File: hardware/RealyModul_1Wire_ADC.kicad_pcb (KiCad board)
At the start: 2 copper layers, 90.2 x 80 mm, 69 parts, among them J1 Conn_01x03, J10 1Wire, J11 1Wire, J2 1Wire, J3 Conn_01x03, J4 Conn_01x03, J5 1Wire, J6 1Wire, J7 1Wire, J8 1Wire, J9 1Wire, K1 RT314A12, K2 RT314A12, K3 RT314A12, Q1 BSS123, Q2 BSS123, Q3 BSS123, U1 LT1129-3.3_SOT223, U2 R-78B5.0-2.0, U3 ESP32-WROOM-32D, U4 ADS1115IDGS

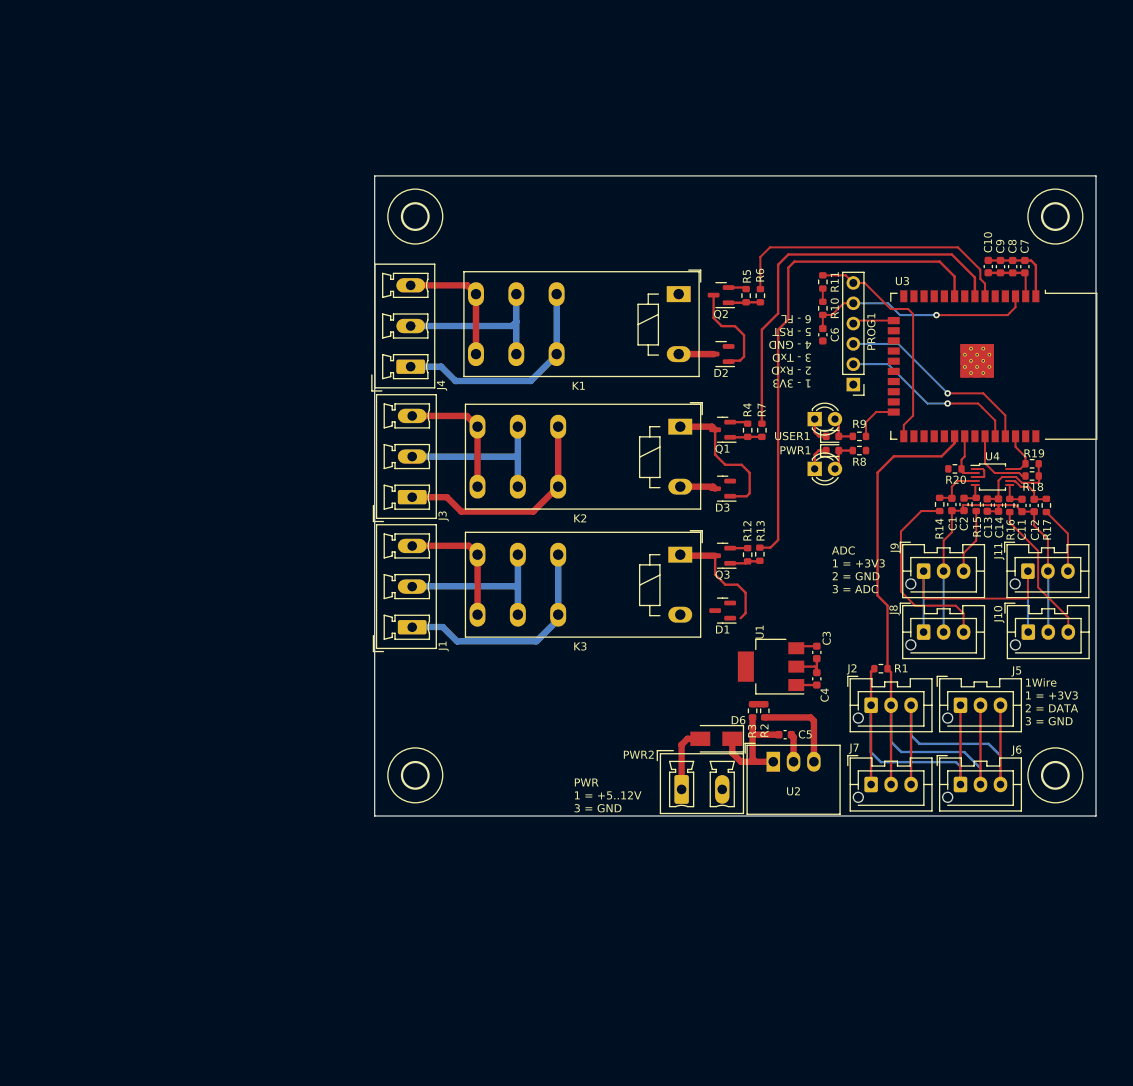
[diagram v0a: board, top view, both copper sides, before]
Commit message: Schaltplan angepasst
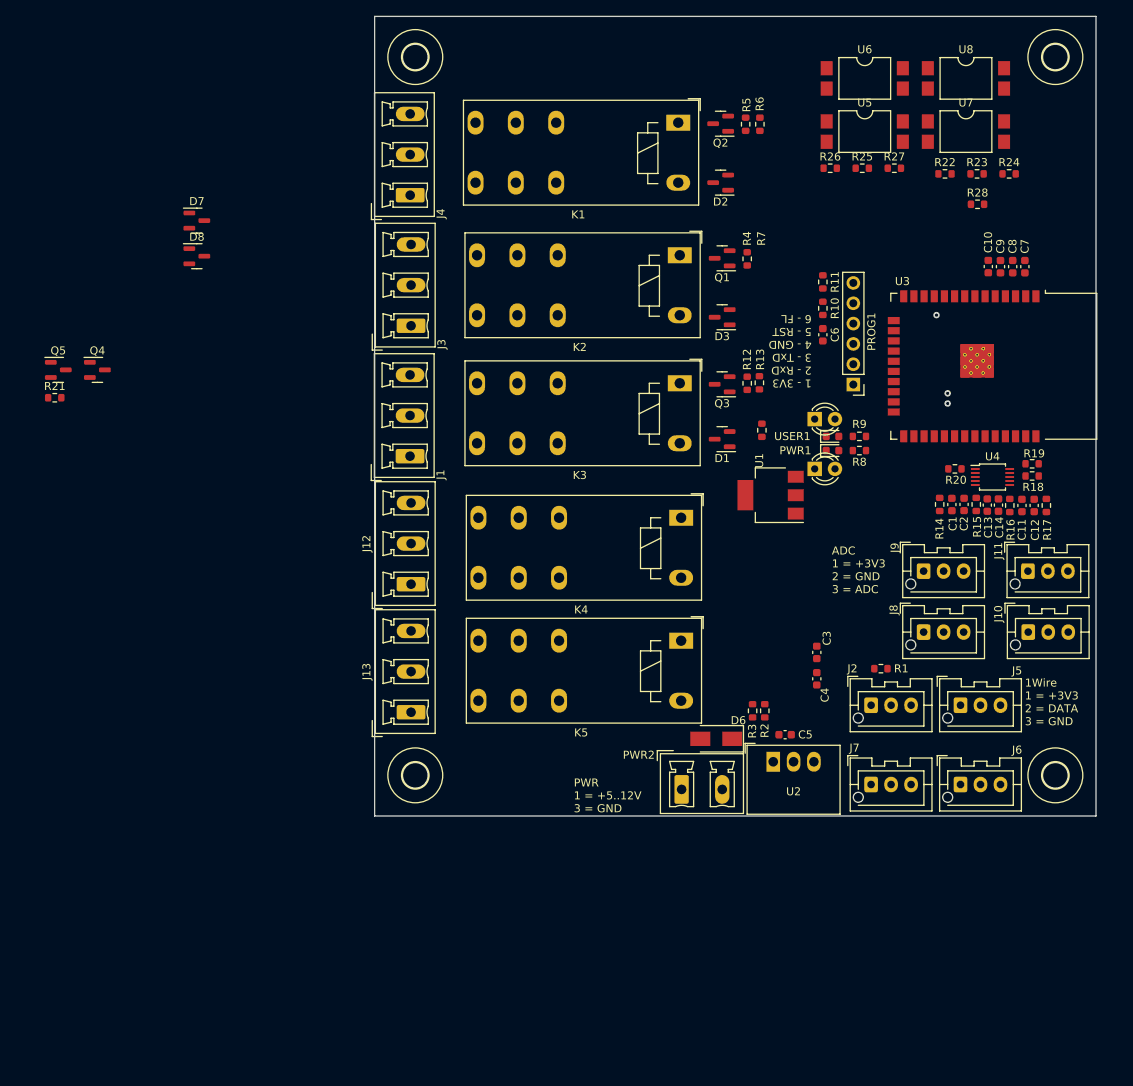
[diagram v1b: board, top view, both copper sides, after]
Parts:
- added D7: BAS21, Package_TO_SOT_SMD:SOT-23, F.Cu at (92.1, 65.3)
- added D8: BAS21, Package_TO_SOT_SMD:SOT-23, F.Cu at (92.1, 69.7)
- added J12: Conn_01x03, Connector_Phoenix_MC_HighVoltage:PhoenixContact_MCV_1,5_3-G-5.08_1x03_P5.08mm_Vertical, F.Cu at (118.9, 110.7)
- added J13: Conn_01x03, Connector_Phoenix_MC_HighVoltage:PhoenixContact_MCV_1,5_3-G-5.08_1x03_P5.08mm_Vertical, F.Cu at (118.9, 126.7)
- added K4: RT314A12, Relay_THT:Relay_SPDT_Schrack-RT1-16A-FormC_RM5mm, F.Cu at (152.6, 102.4)
- added K5: RT314A12, Relay_THT:Relay_SPDT_Schrack-RT1-16A-FormC_RM5mm, F.Cu at (152.6, 117.8)
- added Q4: BSS123, Package_TO_SOT_SMD:SOT-23, F.Cu at (79.6, 83.9)
- added Q5: BSS123, Package_TO_SOT_SMD:SOT-23, F.Cu at (74.8, 83.9)
- added R21: 100k, Resistor_SMD:R_0603_1608Metric, F.Cu at (74.3, 87.4)
- added R22: 100k, Resistor_SMD:R_0603_1608Metric, F.Cu at (185.6, 59.4)
- added R23: 100, Resistor_SMD:R_0603_1608Metric, F.Cu at (189.6, 59.4)
- added R24: 100, Resistor_SMD:R_0603_1608Metric, F.Cu at (193.6, 59.4)
- added R25: 10k, Resistor_SMD:R_0603_1608Metric, F.Cu at (175.3, 58.7)
- added R26: 10k, Resistor_SMD:R_0603_1608Metric, F.Cu at (171.2, 58.7)
- added R27: 10k, Resistor_SMD:R_0603_1608Metric, F.Cu at (179.3, 58.7)
- added R28: 10k, Resistor_SMD:R_0603_1608Metric, F.Cu at (189.7, 63.2)
- added U5: SFH6206-1T, Package_DIP:SMDIP-4_W9.53mm_Clearance8mm, F.Cu at (175.6, 54.1)
- added U6: SFH6206-1T, Package_DIP:SMDIP-4_W9.53mm_Clearance8mm, F.Cu at (175.6, 47.5)
- added U7: SFH6206-1T, Package_DIP:SMDIP-4_W9.53mm_Clearance8mm, F.Cu at (188.2, 54.1)
- added U8: SFH6206-1T, Package_DIP:SMDIP-4_W9.53mm_Clearance8mm, F.Cu at (188.2, 47.5)
- R12: value 100k -> 0R0
- R13: value 100 -> N.P.
- R2: value 0R0 -> 100k
- R3: value N.P. -> 100k
- R5: value 100k -> 100
- moved J3 21.4 mm to (118.9, 78.4)
- moved K1 21.4 mm to (152.3, 53.0)
- moved Q2 21.4 mm to (157.5, 53.2)
- moved R5 21.4 mm to (160.7, 53.2)
- moved R6 21.4 mm to (162.5, 53.2)
- moved D1 21.4 mm to (157.7, 92.6)
- moved D2 21.4 mm to (157.5, 60.5)
- moved D3 21.4 mm to (157.7, 77.4)
- moved K2 21.4 mm to (152.4, 69.6)
- moved K3 21.4 mm to (152.4, 85.6)
- moved Q1 21.4 mm to (157.7, 70.0)
- moved Q3 21.4 mm to (157.7, 85.7)
- moved R12 21.4 mm to (160.9, 85.6)
- moved R13 21.4 mm to (162.4, 85.6)
- moved R4 21.4 mm to (160.9, 70.1)
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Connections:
- K1 pad 11: Net-(J4-Pad2) -> Net-(J1-Pad2)
- K1 pad 12: Net-(J4-Pad1) -> Net-(J1-Pad1)
- K1 pad 14: Net-(J4-Pad3) -> Net-(J1-Pad3)
- K1 pad A1: Net-(D2-Pad1) -> Net-(D1-Pad1)
- K2 pad 11: Net-(J3-Pad2) -> Net-(J4-Pad2)
- K2 pad 12: Net-(J3-Pad1) -> Net-(J4-Pad1)
- K2 pad 14: Net-(J3-Pad3) -> Net-(J4-Pad3)
- K2 pad A1: Net-(D3-Pad1) -> Net-(D2-Pad1)
- K3 pad 11: Net-(J1-Pad2) -> Net-(J3-Pad2)
- K3 pad 12: Net-(J1-Pad1) -> Net-(J3-Pad1)
- K3 pad 14: Net-(J1-Pad3) -> Net-(J3-Pad3)
- K3 pad A1: Net-(D1-Pad1) -> Net-(D3-Pad1)
- Q1 pad 3: Net-(D3-Pad1) -> Net-(D1-Pad1)
- Q3 pad 3: Net-(D1-Pad1) -> Net-(D3-Pad1)
- R12 pad 1: Net-(Q3-Pad1) -> +5V
- R12 pad 2: GND -> Vdrive
- R13 pad 1: Net-(Q3-Pad1) -> +24V
- R13 pad 2: /IO33_K3 -> Vdrive
- R2 pad 1: +5V -> Net-(Q3-Pad1)
- R2 pad 2: Vdrive -> GND
- R3 pad 1: +24V -> Net-(Q2-Pad1)
- R3 pad 2: Vdrive -> GND
- R5 pad 1: Net-(Q2-Pad1) -> Net-(Q3-Pad1)
- R5 pad 2: GND -> /IO33_K3
- R6 pad 2: /IO34_K1 -> /IO35_K2
- R7 pad 2: /IO35_K2 -> /IO34_K1
- U3 pad 10: unconnected-(U3-Pad10) -> /IO25_K5
- U3 pad 11: unconnected-(U3-Pad11) -> /INPUT_01
- U3 pad 12: unconnected-(U3-Pad12) -> /INPUT_02
- U3 pad 13: unconnected-(U3-Pad13) -> /INPUT_03
- U3 pad 14: unconnected-(U3-Pad14) -> /INPUT_04
- U3 pad 8: unconnected-(U3-Pad8) -> /IO33_K3
- U3 pad 9: /IO33_K3 -> /IO32_K4
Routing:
- net GND: track 124.9 -> 0.00 mm
- net +3.3V: track 103.3 -> 0.00 mm
- net /1Wire: track 80.8 -> 0.00 mm
- net /IO33_K3: track 61.6 -> 0.00 mm
- net /IO35_K2: track 49.4 -> 0.00 mm
- net /IO34_K1: track 36.7 -> 0.00 mm
- net /IO0: track 29.0 -> 0.00 mm
- net /RST: track 28.8 -> 0.00 mm
- net Net-(J4-Pad1): track 28.0 -> 0.00 mm
- net Net-(J3-Pad1): track 27.8 -> 0.00 mm
- net Net-(J1-Pad1): track 27.6 -> 0.00 mm
- net /TXD: track 25.3 -> 0.00 mm
- net Net-(J8-Pad3): track 24.7 -> 0.00 mm
- net /RXD: track 22.6 -> 0.00 mm
- net Net-(J4-Pad2): track 20.9 -> 0.00 mm
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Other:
- board size 90.2 x 80 mm -> 90.2 x 99.9 mm

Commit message: änderung
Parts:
- removed D8: BAS21, Package_TO_SOT_SMD:SOT-23
- removed H1, H2, H3, H4: MOUNT-HOLE3.2, main:3,2
- removed J13: Conn_01x03, Connector_Phoenix_MC_HighVoltage:PhoenixContact_MCV_1,5_3-G-5.08_1x03_P5.08mm_Vertical
- removed J6, J7: 1Wire, Connector_JST:JST_XA_B03B-XASK-1-A_1x03_P2.50mm_Vertical
- removed K5: RT314A12, Relay_THT:Relay_SPDT_Schrack-RT1-16A-FormC_RM5mm
- removed Q5: BSS123, Package_TO_SOT_SMD:SOT-23
- removed R22: 100k, Resistor_SMD:R_0603_1608Metric
- removed R24: 100, Resistor_SMD:R_0603_1608Metric
- added PS3: IRM-05-5, Converter_ACDC:Converter_ACDC_MeanWell_IRM-05-xx_THT, F.Cu at (105.4, 93.5)
- D1, D2, D3, D7, Q1, Q2, Q3, Q4, R2, R21, R23, R3, R4, R5, R6, R7: moved to B.Cu
- moved U8 114.8 mm to (108.0, 129.5)
- moved U7 106.3 mm to (107.8, 123.7)
- moved U6 97.5 mm to (108.0, 117.7)
- moved D5 94.7 mm to (90.5, 142.6)
- moved PWR1 94.7 mm to (92.7, 146.6)
- moved USER1 94.7 mm to (92.7, 144.8)
- moved D4 94.7 mm to (90.5, 148.8)
- moved R9 94.7 mm to (96.1, 144.8)
- moved R8 94.7 mm to (96.1, 146.6)
- moved R25 91.5 mm to (115.8, 128.3), turned to 180 degrees
- moved U5 88.8 mm to (108.0, 111.8)
- moved R28 87.6 mm to (116.0, 110.5), turned to 180 degrees
- moved R27 85.7 mm to (116.0, 116.5), turned to 180 degrees
- moved R26 84.4 mm to (115.8, 122.4), turned to 180 degrees
- moved C7 80.2 mm to (156.0, 140.8), turned to 0 degrees
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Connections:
- R23 pad 2: /IO25_K5 -> /IO32_K4
- U3 pad 10: /IO25_K5 -> unconnected-(U3-IO25-Pad10)
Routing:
- net /TXD: vias 1 -> 0
- net /RXD: vias 1 -> 0
- net /RST: vias 1 -> 0
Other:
- board size 90.2 x 99.9 mm -> 86.4 x 103.6 mm

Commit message: fast fertig
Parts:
- removed C5: 100nF/50V, Capacitor_SMD:C_0603_1608Metric
- removed D6: ES1D, Diode_SMD:D_SMA
- removed J11: 1Wire, Connector_JST:JST_XA_B03B-XASK-1-A_1x03_P2.50mm_Vertical
- removed PWR2: Conn_01x02, Connector_Phoenix_MC_HighVoltage:PhoenixContact_MCV_1,5_2-G-5.08_1x02_P5.08mm_Vertical
- removed R13: N.P., Resistor_SMD:R_0603_1608Metric
- removed U2: R-78B5.0-2.0, Converter_DCDC:Converter_DCDC_RECOM_R-78B-2.0_THT
- added J6: Conn_01x03, Connector_Phoenix_MKDSx:MKDSN 2,5-2-5.08, F.Cu at (171.6, 77.8)
- added J7: Conn_01x03, Connector_Phoenix_MKDSx:MKDSN 2,5-2-5.08, F.Cu at (92.7, 107.5)
- added PWR10: Conn_01x03, Connector_Phoenix_MKDSx:MKDSN 2,5-2-5.08, F.Cu at (92.7, 88.6)
- added R200: R, Resistor_SMD:R_2010_5025Metric_Pad1.40x2.65mm_HandSolder, B.Cu at (97.8, 107.4)
- added R201: R, Resistor_SMD:R_2010_5025Metric_Pad1.40x2.65mm_HandSolder, F.Cu at (104.9, 112.5)
- added R202: R, Resistor_SMD:R_2010_5025Metric_Pad1.40x2.65mm_HandSolder, B.Cu at (97.8, 112.5)
- added R203: R, Resistor_SMD:R_2010_5025Metric_Pad1.40x2.65mm_HandSolder, F.Cu at (104.9, 118.6)
- added R204: R, Resistor_SMD:R_2010_5025Metric_Pad1.40x2.65mm_HandSolder, B.Cu at (97.8, 117.5)
- added R205: R, Resistor_SMD:R_2010_5025Metric_Pad1.40x2.65mm_HandSolder, F.Cu at (105.0, 124.6)
- added R206: R, Resistor_SMD:R_2010_5025Metric_Pad1.40x2.65mm_HandSolder, B.Cu at (97.8, 122.4)
- added R207: R, Resistor_SMD:R_2010_5025Metric_Pad1.40x2.65mm_HandSolder, F.Cu at (105.0, 130.3)
- J1, J12, J3, J4: footprint Connector_Phoenix_MC_HighVoltage:PhoenixContact_MCV_1,5_3-G-5.08_1x03_P5.08mm_Vertical -> Connector_Phoenix_MKDSx:MKDSN 2,5-2-5.08
- J10, J8, J9: value 1Wire -> Conn_01x04; footprint Connector_JST:JST_XA_B03B-XASK-1-A_1x03_P2.50mm_Vertical -> Connector_Phoenix_MC:PhoenixContact_MCV_1,5_4-G-3.81_1x04_P3.81mm_Vertical
- J2, J5: value 1Wire -> Conn_01x03; footprint Connector_JST:JST_XA_B03B-XASK-1-A_1x03_P2.50mm_Vertical -> Connector_Phoenix_MKDSx:MKDSN 2,5-2-5.08
- R12: moved to B.Cu
- moved J12 91.1 mm to (92.7, 117.5)
- moved J2 83.7 mm to (92.7, 62.3)
- moved J10 83.1 mm to (92.3, 149.2)
- moved J4 80.7 mm to (171.6, 57.8)
- moved J3 80.0 mm to (92.7, 72.3)
- moved R1 79.0 mm to (102.5, 146.6), turned to -90 degrees
- moved D5 57.1 mm to (139.8, 113.9), turned to -90 degrees
- moved D4 55.5 mm to (133.6, 113.9), turned to -90 degrees
- moved USER1 53.3 mm to (137.7, 116.1), turned to -90 degrees
- moved PWR1 52.8 mm to (135.9, 116.1), turned to -90 degrees
- moved R9 48.7 mm to (137.7, 119.5), turned to 90 degrees
- moved R8 48.2 mm to (135.9, 119.5), turned to 90 degrees
- moved R28 44.3 mm to (157.7, 125.2)
- moved R27 43.0 mm to (157.7, 126.7)
- moved R26 42.3 mm to (157.7, 128.3)
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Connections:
- J10 pad 3: Net-(J10-Pin_3) -> /1Wire
- J2 pad 1: +3.3V -> Net-(J2-Pin_1)
- J2 pad 2: /1Wire -> Net-(J2-Pin_2)
- J5 pad 1: +3.3V -> Net-(J5-Pin_1)
- J5 pad 2: /1Wire -> Net-(J5-Pin_2)
- K1 pad 12: Net-(J1-Pin_1) -> Net-(J2-Pin_1)
- K1 pad 14: Net-(J1-Pin_3) -> Net-(J1-Pin_1)
- K2 pad 11: Net-(J4-Pin_2) -> Net-(J3-Pin_1)
- K2 pad 12: Net-(J4-Pin_1) -> Net-(J3-Pin_2)
- K2 pad 14: Net-(J4-Pin_3) -> Net-(J2-Pin_2)
- K3 pad 11: Net-(J3-Pin_2) -> Net-(J4-Pin_1)
- K3 pad 12: Net-(J3-Pin_1) -> Net-(J5-Pin_2)
- K3 pad 14: Net-(J3-Pin_3) -> Net-(J4-Pin_2)
- K4 pad 11: Net-(J12-Pin_2) -> Net-(J6-Pin_2)
- K4 pad 12: Net-(J12-Pin_1) -> Net-(J6-Pin_1)
- K4 pad 14: Net-(J12-Pin_3) -> Net-(J5-Pin_1)
- PS3 pad 1: GND -> /POWER_N
- R15 pad 1: Net-(J9-Pin_3) -> Net-(J8-Pin_4)
- R16 pad 1: Net-(J10-Pin_3) -> Net-(J9-Pin_3)
- R17 pad 1: Net-(J11-Pin_3) -> Net-(J9-Pin_4)
- R25 pad 2: /INPUT_04 -> /INPUT_01
- R26 pad 2: /INPUT_03 -> /INPUT_02
- R27 pad 2: /INPUT_02 -> /INPUT_03
- R28 pad 2: /INPUT_01 -> /INPUT_04
- U5 pad 1: unconnected-(U5-Pad1) -> Net-(R200-Pad2)
- U5 pad 2: unconnected-(U5-Pad2) -> Net-(R201-Pad2)
- U5 pad 4: /INPUT_01 -> /INPUT_04
- U6 pad 1: unconnected-(U6-Pad1) -> Net-(R202-Pad2)
- U6 pad 2: unconnected-(U6-Pad2) -> Net-(R203-Pad2)
- U6 pad 4: /INPUT_02 -> /INPUT_03
- U7 pad 1: unconnected-(U7-Pad1) -> Net-(R204-Pad2)
- U7 pad 2: unconnected-(U7-Pad2) -> Net-(R205-Pad2)
- U7 pad 4: /INPUT_03 -> /INPUT_02
- U8 pad 1: unconnected-(U8-Pad1) -> Net-(R206-Pad2)
- U8 pad 2: unconnected-(U8-Pad2) -> Net-(R207-Pad2)
- U8 pad 4: /INPUT_04 -> /INPUT_01
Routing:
- net +3.3V: track 0.00 -> 209.9 mm, vias 0 -> 3
- net Vdrive: track 0.00 -> 90.9 mm, vias 0 -> 1
- net /IO34_K1: track 0.00 -> 89.4 mm, vias 0 -> 3
- net /IO33_K3: track 0.00 -> 82.1 mm, vias 0 -> 3
- net /IO35_K2: track 0.00 -> 71.9 mm, vias 0 -> 1
- net GND: track 0.00 -> 65.1 mm, vias 0 -> 28
- net /IO32_K4: track 0.00 -> 63.6 mm, vias 0 -> 1
- net /1Wire: track 0.00 -> 57.3 mm, vias 0 -> 2
- net /INPUT_04: track 0.00 -> 54.4 mm, vias 0 -> 2
- net /POWER_N: track 0.00 -> 52.4 mm
- net /INPUT_03: track 0.00 -> 49.3 mm, vias 0 -> 2
- net /INPUT_02: track 0.00 -> 44.2 mm, vias 0 -> 2
- net /SCL: track 0.00 -> 42.5 mm
- net /SDA: track 0.00 -> 41.2 mm, vias 0 -> 2
- net /INPUT_01: track 0.00 -> 39.9 mm, vias 0 -> 2
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- added copper zone on B.Cu, net GND
- added copper zone on F.Cu, net GND
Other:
- board text removed: "PWR 1 = +5..12V 3 = GND"

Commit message: fertig
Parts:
- removed PS3: IRM-05-5, Converter_ACDC:Converter_ACDC_MeanWell_IRM-05-xx_THT
- added J11: Conn_01x02, Connector_Phoenix_MKDSx:MKDS_1_2_3.81, F.Cu at (172.0, 108.3)
- added J13: Conn_01x02, Connector_Phoenix_MKDSx:MKDS_1_2_3.81, F.Cu at (172.0, 115.9)
- added PS1: IRM-05-5, Converter_ACDC:Converter_ACDC_MeanWell_IRM-05-xx_THT, F.Cu at (105.4, 93.5)
- J10: value Conn_01x04 -> Conn_01x03; footprint Connector_Phoenix_MC:PhoenixContact_MCV_1,5_4-G-3.81_1x04_P3.81mm_Vertical -> Connector_Phoenix_MKDSx:MKDS_1_3_3.81
- J8, J9: value Conn_01x04 -> Conn_01x02; footprint Connector_Phoenix_MC:PhoenixContact_MCV_1,5_4-G-3.81_1x04_P3.81mm_Vertical -> Connector_Phoenix_MKDSx:MKDS_1_2_3.81
- R1: value 4K7 -> 4k7
- moved J9 28.4 mm to (172.0, 133.0), turned to 90 degrees
- moved J10 7.65 mm to (91.5, 141.6), turned to -90 degrees
- moved J8 3.81 mm to (172.0, 125.3), turned to 90 degrees
- moved R1 1.71 mm to (102.5, 144.8)
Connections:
- J8 pad 1: +3.3V -> GND
- J8 pad 2: GND -> +3.3V
- J9 pad 1: +3.3V -> Net-(J9-Pin_1)
- J9 pad 2: GND -> Net-(J9-Pin_2)
- R1 pad 1: /1Wire -> +3.3V
- R1 pad 2: +3.3V -> /1Wire
- R14 pad 1: Net-(J8-Pin_3) -> Net-(J9-Pin_2)
- R15 pad 1: Net-(J8-Pin_4) -> Net-(J9-Pin_1)
- R16 pad 1: Net-(J9-Pin_3) -> Net-(J13-Pin_2)
- R17 pad 1: Net-(J9-Pin_4) -> Net-(J13-Pin_1)
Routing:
- net Net-(J9-Pin_1): track 0.00 -> 30.9 mm
- net Net-(J8-Pin_4): track 30.9 -> 0.00 mm
- net Net-(J9-Pin_4): track 23.5 -> 0.00 mm
- net Net-(J13-Pin_1): track 0.00 -> 23.5 mm
- net Net-(J9-Pin_2): track 0.00 -> 18.2 mm
- net Net-(J8-Pin_3): track 18.2 -> 0.00 mm
- net Net-(J9-Pin_3): track 13.7 -> 0.00 mm
- net Net-(J13-Pin_2): track 0.00 -> 13.7 mm
- net +3.3V: track 209.9 -> 217.6 mm
- net Net-(U4-AIN0): track 4.20 -> 5.75 mm
- net Net-(U4-AIN3): track 4.44 -> 5.99 mm
- net /1Wire: track 57.3 -> 56.3 mm
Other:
- board text added: "1Wire 1 = +3V3 2 = GND 3 = DATA"
- board text added: "AI1 AI0 GND VCC"
- board text added: "AI3 AI2 GND VCC"
- board text added: "L"
- board text added: "N"
- board text added: "VCC Gnd 1W"
- board text removed: "1Wire 1 = +3V3 2 = DATA 3 = GND"
- board text removed: "ADC 1 = +3V3 2 = GND 3 = ADC"

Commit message: create gerber file
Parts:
- moved D5 0.89 mm to (140.7, 113.9)
- moved D4 0.76 mm to (132.8, 113.9)
- moved C11 0.28 mm to (157.7, 111.5)
- moved C12 0.28 mm to (157.7, 110.0)
- moved R16 0.28 mm to (157.7, 113.0)
- moved R17 0.28 mm to (157.7, 108.5)
- moved C1 0.25 mm to (157.7, 120.8)
- moved C2 0.25 mm to (157.7, 119.3)
- moved R14 0.25 mm to (157.7, 122.3)
- moved R15 0.25 mm to (157.7, 117.7)
- moved C14 0.17 mm to (157.7, 114.6)
- moved C13 0.08 mm to (157.7, 116.1)
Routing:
- net Net-(U4-AIN3): track 5.99 -> 6.64 mm
- net Net-(U4-AIN0): track 5.75 -> 6.27 mm
